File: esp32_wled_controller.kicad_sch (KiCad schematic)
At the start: 98 parts, among them J2 Screw_Terminal_01x03, J3 Screw_Terminal_01x03, J4 Screw_Terminal_01x03, J5 Screw_Terminal_01x03, J6 Screw_Terminal_01x02, J7 Screw_Terminal_01x02, J9 USB_C_Receptacle_USB2.0_16P, K1 SRD-05VDC-SL-C, K2 SRD-05VDC-SL-C, K3 SRD-05VDC-SL-C, K4 SRD-05VDC-SL-C, Q3 SS8050, Q4 SS8050, Q5 SS8050, Q6 SS8050, SW1 SW_SPST, SW2 SW_SPST, SW3 SS12D10G4 071, U1 ESP32-S3FH4R2, U10 USBLC6-2P6, U11 TLV76733DRVx, U2 LMR51430, U4 EL817, U5 EL817, U6 EL817, U7 EL817, U9 SN74AHCT125PWR, Y1 ECS-400-10-37B2-CKM-TR

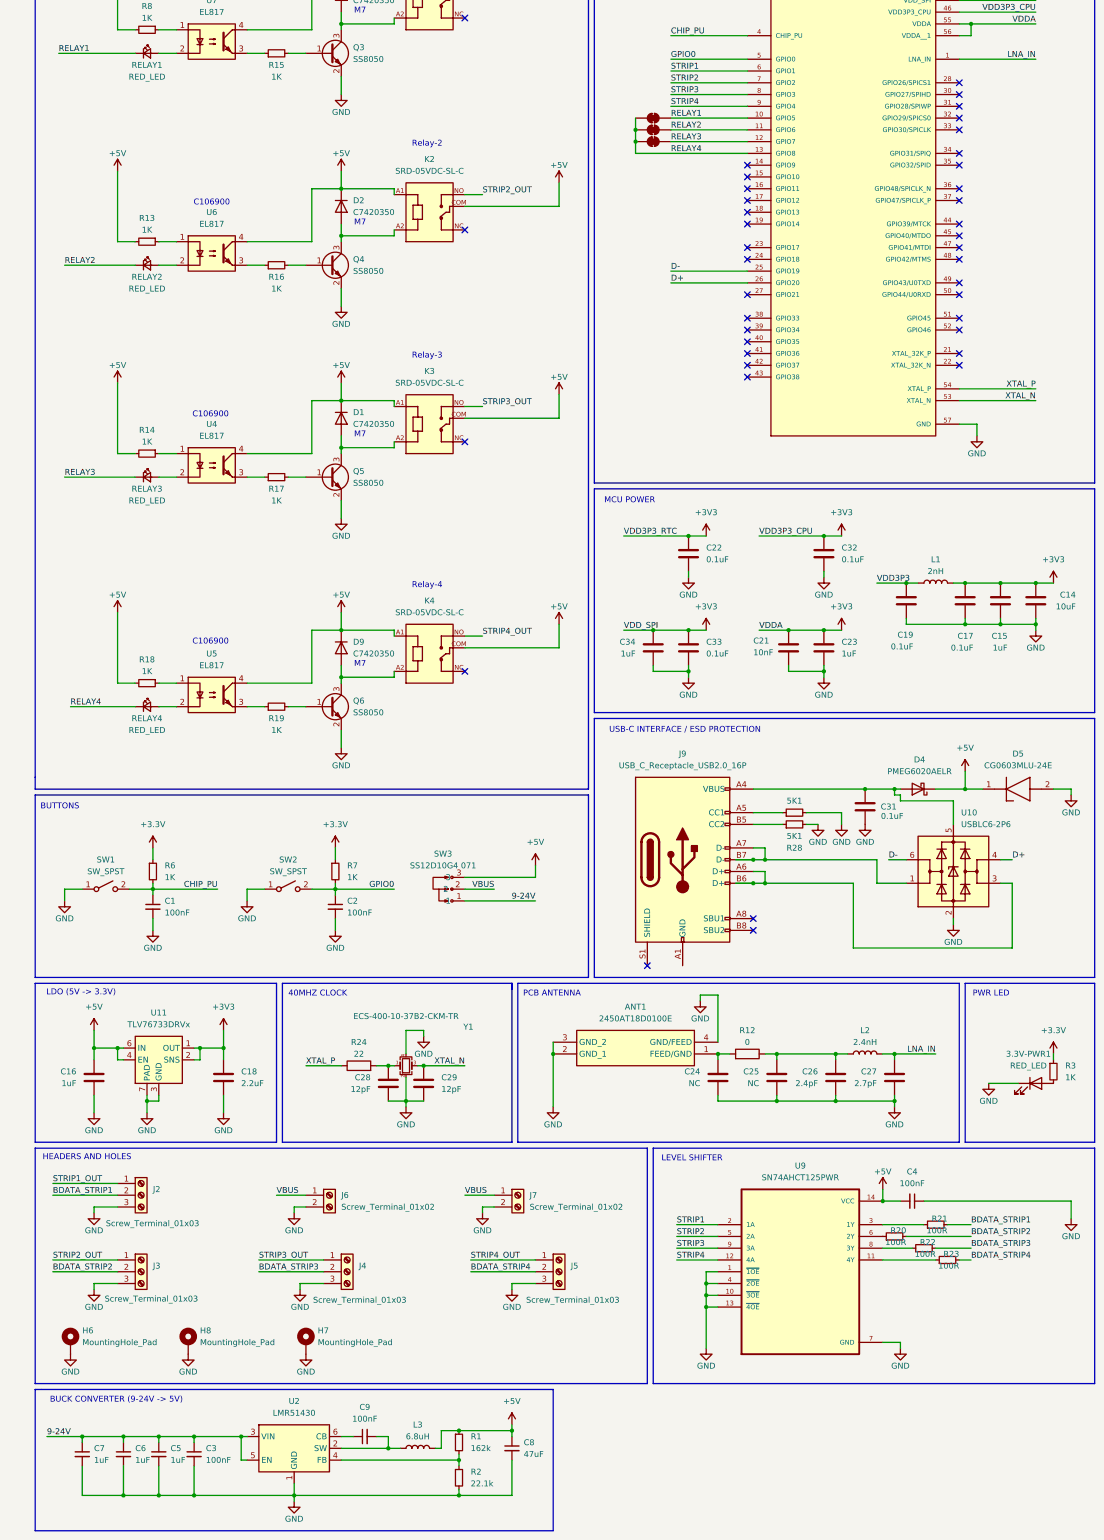
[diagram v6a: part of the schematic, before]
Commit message: add pcb antenna
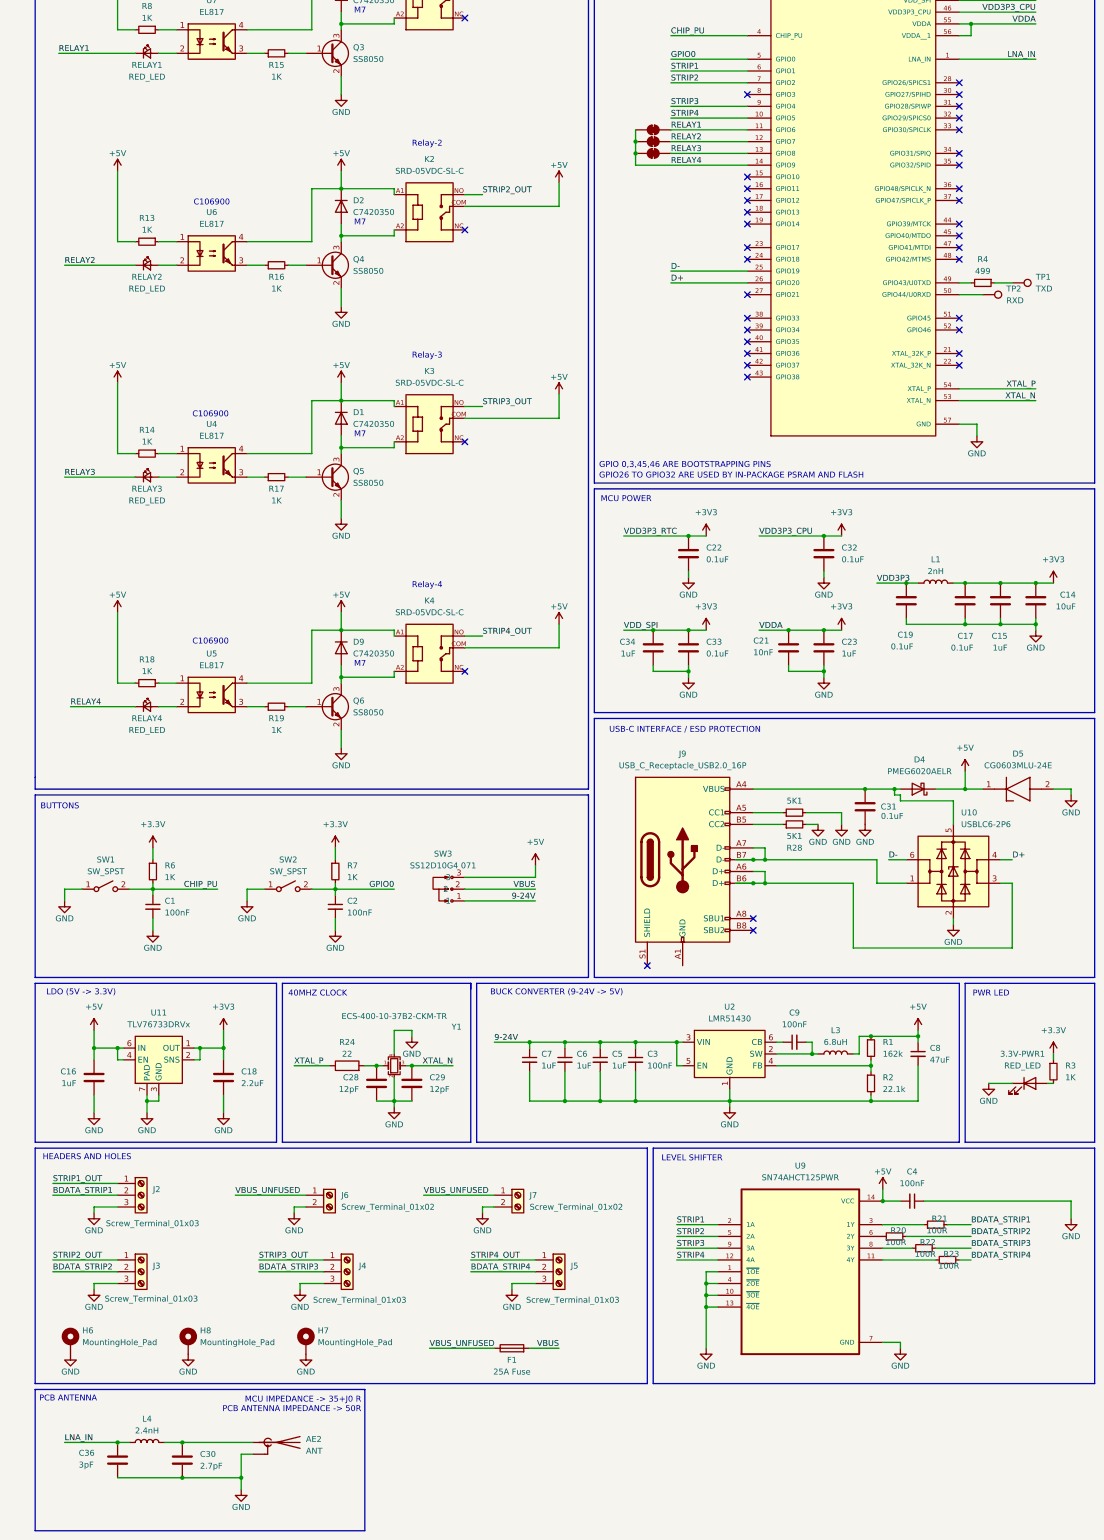
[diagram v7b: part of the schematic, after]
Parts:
- removed ANT1: 2450AT18D0100E, lib:ANT-SMD_4P-L3.2-W1.6, symbol 2450AT18D0100E:2450AT18D0100E
- removed C24, C25: NC, Capacitor_SMD:C_0201_0603Metric_Pad0.64x0.40mm_HandSolder, symbol Device:C
- removed C26: 2.4pF, Capacitor_SMD:C_0201_0603Metric_Pad0.64x0.40mm_HandSolder, symbol Device:C
- removed C27: 2.7pF, Capacitor_SMD:C_0201_0603Metric_Pad0.64x0.40mm_HandSolder, symbol Device:C
- removed L2: 2.4nH, Inductor_SMD:L_0201_0603Metric, symbol Device:L
- removed R12: 0, Resistor_SMD:R_0201_0603Metric, symbol Device:R
- added AE2: ANT, RF_Antenna:Texas_SWRA117D_2.4GHz_Right, symbol Device:Antenna_Shield
- added C30: 2.7pF, Capacitor_SMD:C_0201_0603Metric_Pad0.64x0.40mm_HandSolder, symbol Device:C
- added C36: 3pF, Capacitor_SMD:C_0201_0603Metric_Pad0.64x0.40mm_HandSolder, symbol Device:C
- added F1: 25A Fuse, Fuse:Fuseholder_Blade_Mini_Keystone_3568, symbol Device:Fuse
- added L4: 2.4nH, Inductor_SMD:L_0201_0603Metric, symbol Device:L
- added R4: 499, Resistor_SMD:R_0402_1005Metric_Pad0.72x0.64mm_HandSolder, symbol Device:R_Small
- added TP1: TXD, symbol Connector:TestPoint
- added TP2: RXD, symbol Connector:TestPoint
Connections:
- net GND: now also AE2.2 (Shield), C30.2, C36.2
- net LNA_IN: now also C36.1, L4.2
- net RELAY1: now also U1.11 (GPIO6); no longer U1.10 (GPIO5)
- net RELAY2: now also U1.12 (GPIO7); no longer U1.11 (GPIO6)
- net RELAY3: now also U1.13 (GPIO8); no longer U1.12 (GPIO7)
- net RELAY4: now also U1.14 (GPIO9); no longer U1.13 (GPIO8)
- net STRIP3: now also U1.9 (GPIO4); no longer U1.8 (GPIO3)
- net STRIP4: now also U1.10 (GPIO5); no longer U1.9 (GPIO4)
- net VBUS: now also F1.2; no longer J6.1 (Pin_1), J7.1 (Pin_1)
- net at U1.49 (GPIO43/U0TXD): now also R4.2
- net at U1.50 (GPIO44/U0RXD): now also TP2.1
- new net: AE2.1 (A), C30.1, L4.1
- new net: R4.1, TP1.1
- new net VBUS_UNFUSED: F1.1, J6.1 (Pin_1), J7.1 (Pin_1)
- no-connect marks 41 -> 39
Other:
- note added: "GPIO 0,3,45,46 ARE BOOTSTRAPPING PINS"
- note added: "GPIO26 TO GPIO32 ARE USED BY IN-PACKAGE PSRAM AND FLASH"
- note added: "MCU IMPEDANCE -> 35+J0 R PCB ANTENNA IMPEDANCE -> 50R"
- moved on the sheet: 3.3V-PWR1, C28, C29, C3, C5, C6, C7, C8, C9, L3, R1, R2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

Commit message: inital rev 1.3 pcb design
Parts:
- added F1, F3, F4: 10A Fuse, Fuse:Fuseholder_Blade_Mini_Keystone_3568, symbol Device:Fuse
- AE2: footprint RF_Antenna:Texas_SWRA117D_2.4GHz_Right -> RF_Antenna:Texas_SWRA117D_2.4GHz_Left
- F2: renamed from F1; value 25A Fuse -> 10A Fuse
- H6, H7, H8: value MountingHole_Pad -> MountingHole
- J6: value Screw_Terminal_01x02 -> VBUS_INPUT1
- J7: value Screw_Terminal_01x02 -> VBUS_INPUT2
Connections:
- net STRIP1_OUT: now also F1.2; no longer K1.NO
- net STRIP2_OUT: now also F2.2; no longer K2.NO
- net STRIP3_OUT: now also F3.2; no longer J4.1 (Pin_1), K3.NO
- net STRIP4_OUT: now also F4.2; no longer K4.NO
- net VBUS: now also J6.1 (Pin_1), J7.1 (Pin_1); no longer F2.2
- net USB_D-: now reaches J9.A7 (D-), J9.B7 (D-), U10.1 (I/O1)
- net USB_D+: now reaches J9.A6 (D+), J9.B6 (D+), U10.3 (I/O2)
- removed net VBUS_UNFUSED: F2.1, J6.1 (Pin_1), J7.1 (Pin_1)
- new net STRIP1_OUT_UF: F1.1, K1.NO
- new net STRIP2_OUT_UF: F2.1, K2.NO
- new net STRIP3_OUT_UF: F3.1, K3.NO
- new net STRIP4_OUT_UF: F4.1, K4.NO
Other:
- note added: "HEADERS, FUSES AND HOLES"
- note removed: "HEADERS AND HOLES"
- moved on the sheet: C4, F2, H6, H7, H8, J4, J5, J6, J7, R20, R21, R22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
